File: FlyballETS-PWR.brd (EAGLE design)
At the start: 48.3 x 50.8 mm, 8 parts

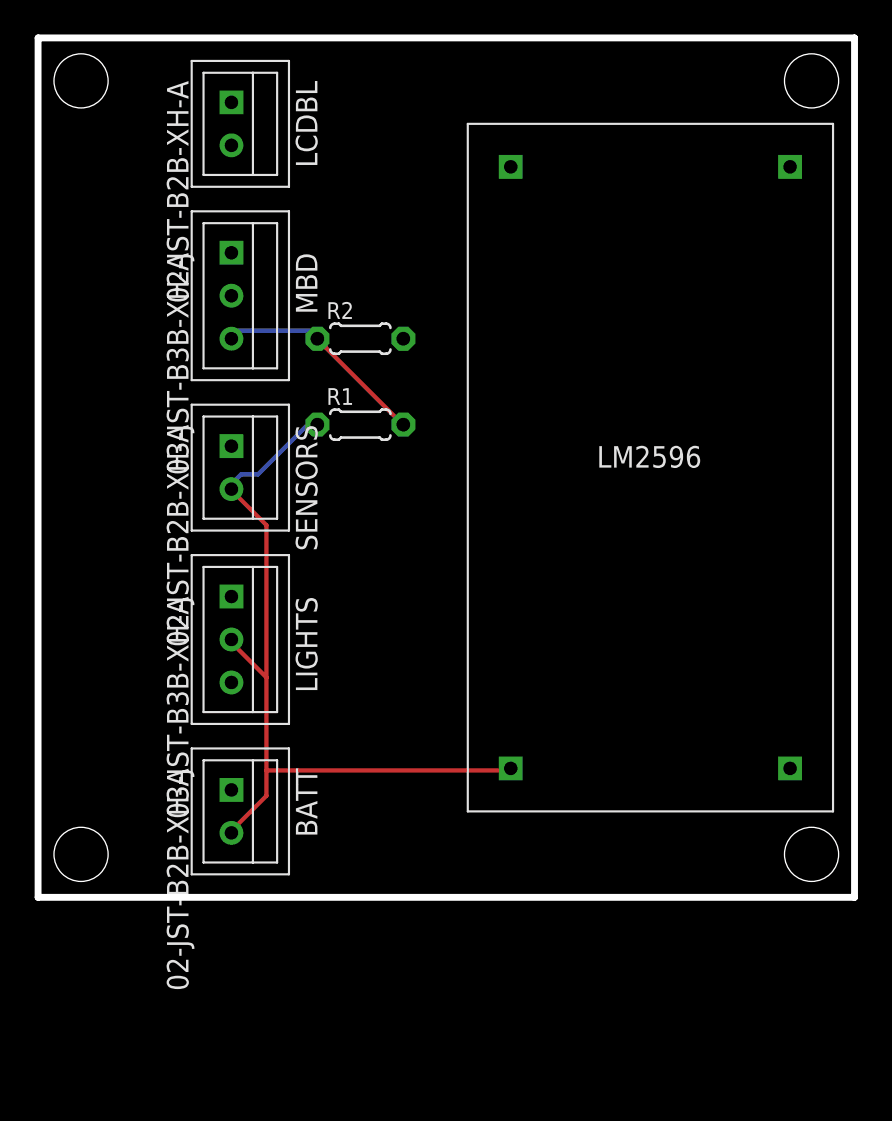
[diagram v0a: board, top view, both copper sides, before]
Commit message: Updated drawings and added PNG exports
- Added frames around drawings to make it look neater
- Added PNG export files so people who don't have EAGLE can see
everything
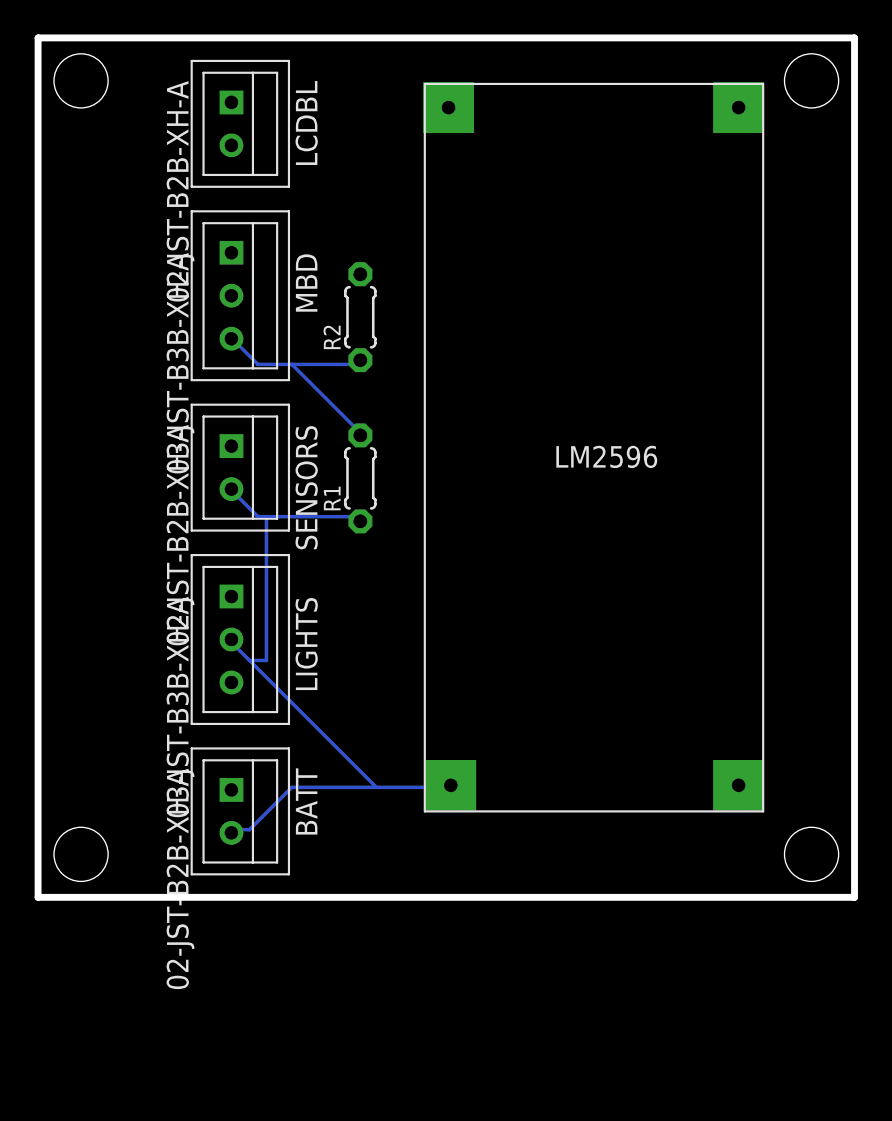
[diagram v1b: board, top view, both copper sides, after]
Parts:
- removed U$3: LM2596-BOARD, _custom:LM2596-BOARD
- added U$1: LM2596-BOARD, _custom:LM2596-BOARD
- added U$2: (no value), frames:A5L-LOC
- moved R1 3.18 mm to (19.1, 24.8), turned to 90 degrees
- moved R2 1.27 mm to (19.1, 34.3), turned to 90 degrees
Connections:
- net +12V: now also U$1.VIN; no longer U$3.VIN
- net +5V: now also U$1.VOUT; no longer U$3.VOUT
- net GND: now also U$1.GND@1, U$1.GND@2; no longer U$3.GND@1, U$3.GND@2
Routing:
- net +12V: track 46.4 -> 44.5 mm
- net N$1: track 13.4 -> 14.3 mm
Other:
- board text added: "Alex Goris"
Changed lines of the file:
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@@
 http://bit.ly/1ErZ5QD
 LICENSE: CC-BY-SA</text>
+<text x="77.47" y="-27.94" size="2.54" layer="48">Alex Goris</text>
+<text x="25.4" y="-40.64" size="2.54" layer="48">FlyballETS
+PowerBoard v1
+http://bit.ly/1ErZ5QD
+LICENSE: CC-BY-SA</text>
+<dimension x1="48.26" y1="0" x2="48.26" y2="50.8" x3="58.42" y3="25.4" textsize="1.778" layer="48"/>
+<dimension x1="48.26" y1="50.8" x2="0" y2="50.8" x3="24.13" y3="60.96" textsize="1.778" layer="48"/>
 </plain>
 <attributes>
@@
 <element name="LIGHTS" library="bt_con-jst-xh" package="B3B-XH" value="03-JST-B3B-XH-A" x="11.43" y="15.24" rot="R270"/>
 <element name="MBD" library="bt_con-jst-xh" package="B3B-XH" value="03-JST-B3B-XH-A" x="11.43" y="35.56" rot="R270"/>
-<element name="R1" library="resistor" package="0204/5" value="70k" x="19.05" y="27.94"/>
-<element name="R2" library="resistor" package="0204/5" value="50k" x="19.05" y="33.02"/>
+<element name="R1" library="resistor" package="0204/5" value="70k" x="19.05" y="24.765" rot="R90"/>
+<element name="R2" library="resistor" package="0204/5" value="50k" x="19.05" y="34.29" rot="R90"/>
 <element name="SENSORS" library="bt_con-jst-xh" package="B2B-XH" value="02-JST-B2B-XH-A" x="11.43" y="24.13" rot="R270"/>
-<element name="U$3" library="_custom" package="LM2596-BOARD" value="LM2596-BOARD" x="25.4" y="5.08"/>
+<element name="U$1" library="_custom" package="LM2596-BOARD" value="LM2596-BOARD" x="22.86" y="5.08"/>
+<element name="U$2" library="frames" package="A5L-LOC" value="" x="-63.5" y="-48.26"/>
 </elements>
 <signals>
 <signal name="+5V">
-<contactref element="U$3" pad="VOUT"/>
 <contactref element="LIGHTS" pad="P$3"/>
 <contactref element="MBD" pad="P$2"/>
@@
 <vertex x="0" y="0"/>
 </polygon>
+<contactref element="U$1" pad="VOUT"/>
 </signal>
 <signal name="GND">
 <contactref element="BATT" pad="P$1"/>
-<contactref element="U$3" pad="GND@1"/>
 <contactref element="SENSORS" pad="P$1"/>
 <contactref element="LIGHTS" pad="P$1"/>
@@
 <contactref element="R2" pad="2"/>
 <contactref element="LCDBL" pad="P$1"/>
-<contactref element="U$3" pad="GND@2"/>
 <polygon width="0.4064" layer="16">
 <vertex x="0" y="50.8"/>
@@
 <vertex x="0" y="0"/>
 </polygon>
+<contactref element="U$1" pad="GND@1"/>
+<contactref element="U$1" pad="GND@2"/>
 </signal>
 <signal name="+12V">
 <contactref element="BATT" pad="P$2"/>
-<contactref element="U$3" pad="VIN"/>
 <contactref element="SENSORS" pad="P$2"/>
 <contactref element="LIGHTS" pad="P$2"/>
 <contactref element="R1" pad="1"/>
-<wire x1="12" y1="25" x2="11.5" y2="24.5" width="0.254" layer="16"/>
-<wire x1="13" y1="25" x2="12" y2="25" width="0.254" layer="16"/>
-<wire x1="16" y1="28" x2="13" y2="25" width="0.254" layer="16"/>
-<wire x1="16.5" y1="28" x2="16" y2="28" width="0.254" layer="16"/>
-<wire x1="11.5" y1="24.5" x2="11.43" y2="24.13" width="0.254" layer="16"/>
-<wire x1="16.5" y1="28" x2="16.51" y2="27.94" width="0.254" layer="16"/>
-<wire x1="13.5" y1="6" x2="11.5" y2="4" width="0.254" layer="1"/>
-<wire x1="13.5" y1="13" x2="13.5" y2="7.5" width="0.254" layer="1"/>
-<wire x1="13.5" y1="7.5" x2="13.5" y2="6" width="0.254" layer="1"/>
-<wire x1="11.5" y1="15" x2="13.5" y2="13" width="0.254" layer="1"/>
-<wire x1="11.5" y1="4" x2="11.43" y2="3.81" width="0.254" layer="1"/>
-<wire x1="11.5" y1="15" x2="11.43" y2="15.24" width="0.254" layer="1"/>
-<wire x1="13.5" y1="7.5" x2="27.5" y2="7.5" width="0.254" layer="1"/>
-<wire x1="27.5" y1="7.5" x2="27.94" y2="7.62" width="0.254" layer="1"/>
-<wire x1="13.5" y1="22" x2="11.5" y2="24" width="0.254" layer="1"/>
-<wire x1="13.5" y1="13" x2="13.5" y2="22" width="0.254" layer="1"/>
-<wire x1="11.5" y1="24" x2="11.43" y2="24.13" width="0.254" layer="1"/>
+<contactref element="U$1" pad="VIN"/>
+<wire x1="13" y1="22.5" x2="11.5" y2="24" width="0.2032" layer="16"/>
+<wire x1="19" y1="22.5" x2="13.5" y2="22.5" width="0.2032" layer="16"/>
+<wire x1="13.5" y1="22.5" x2="13" y2="22.5" width="0.2032" layer="16"/>
+<wire x1="11.5" y1="24" x2="11.43" y2="24.13" width="0.2032" layer="16"/>
+<wire x1="19" y1="22.5" x2="19.05" y2="22.225" width="0.2032" layer="16"/>
+<wire x1="12.5" y1="4" x2="11.5" y2="4" width="0.2032" layer="16"/>
+<wire x1="15" y1="6.5" x2="12.5" y2="4" width="0.2032" layer="16"/>
+<wire x1="24" y1="6.5" x2="20" y2="6.5" width="0.2032" layer="16"/>
+<wire x1="20" y1="6.5" x2="15" y2="6.5" width="0.2032" layer="16"/>
+<wire x1="11.5" y1="4" x2="11.43" y2="3.81" width="0.2032" layer="16"/>
+<wire x1="24" y1="6.5" x2="24.4" y2="6.62" width="0.2032" layer="16"/>
+<wire x1="20" y1="6.5" x2="12.5" y2="14" width="0.2032" layer="16"/>
+<wire x1="12.5" y1="14" x2="11.5" y2="15" width="0.2032" layer="16"/>
+<wire x1="11.5" y1="15" x2="11.43" y2="15.24" width="0.2032" layer="16"/>
+<wire x1="13.5" y1="14" x2="13.5" y2="22.5" width="0.2032" layer="16"/>
+<wire x1="12.5" y1="14" x2="13.5" y2="14" width="0.2032" layer="16"/>
 </signal>
 <signal name="N$1">
@@
 <contactref element="R2" pad="1"/>
 <contactref element="MBD" pad="P$3"/>
-<wire x1="16.5" y1="33.5" x2="11.5" y2="33.5" width="0.254" layer="16"/>
-<wire x1="11.5" y1="33.5" x2="11.43" y2="33.02" width="0.254" layer="16"/>
-<wire x1="16.5" y1="33.5" x2="16.51" y2="33.02" width="0.254" layer="16"/>
-<wire x1="17" y1="32.5" x2="21.5" y2="28" width="0.254" layer="1"/>
-<wire x1="17" y1="33" x2="17" y2="32.5" width="0.254" layer="1"/>
-<wire x1="21.5" y1="28" x2="21.59" y2="27.94" width="0.254" layer="1"/>
-<wire x1="17" y1="33" x2="16.51" y2="33.02" width="0.254" layer="1"/>
+<wire x1="13" y1="31.5" x2="11.5" y2="33" width="0.2032" layer="16"/>
+<wire x1="19" y1="31.5" x2="15" y2="31.5" width="0.2032" layer="16"/>
+<wire x1="15" y1="31.5" x2="13" y2="31.5" width="0.2032" layer="16"/>
+<wire x1="11.5" y1="33" x2="11.43" y2="33.02" width="0.2032" layer="16"/>
+<wire x1="19" y1="31.5" x2="19.05" y2="31.75" width="0.2032" layer="16"/>
+<wire x1="15" y1="31.5" x2="19" y2="27.5" width="0.2032" layer="16"/>
+<wire x1="19" y1="27.5" x2="19.05" y2="27.305" width="0.2032" layer="16"/>
 </signal>
 </signals>

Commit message: v2 release of remaining boards.
- Lightsboard: Corrected swapped pin connections on L2 side and made
smaller
- Powerboard: Made smaller and added descriptions for LM2596 board
- Sensorboard: Made smaller
- All boards: Removed JST connector type names
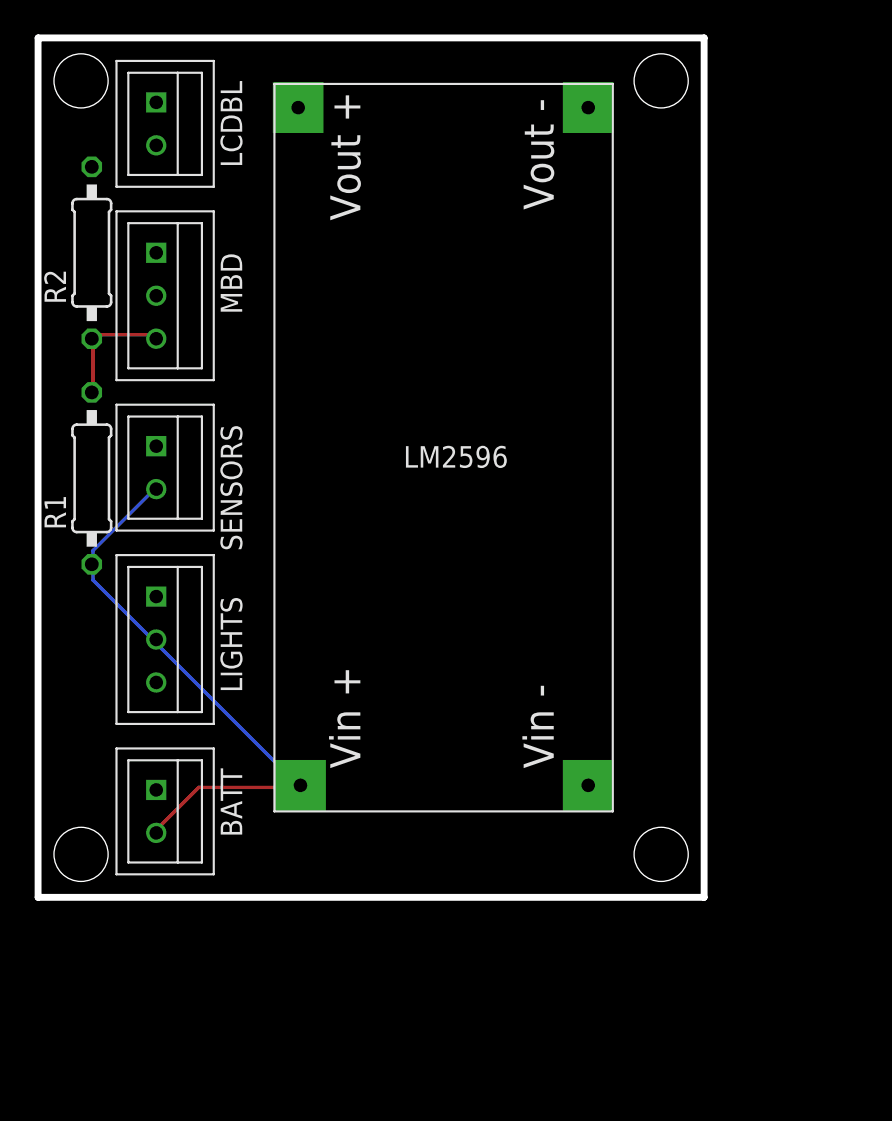
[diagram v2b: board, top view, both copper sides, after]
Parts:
- R1, R2: device resistor:0204/5 -> resistor:0207/10
- moved R2 16.3 mm to (3.17, 38.1)
- moved R1 15.9 mm to (3.17, 24.8)
- moved U$1 8.89 mm to (14.0, 5.08)
- moved BATT 4.44 mm to (6.99, 3.81)
- moved LCDBL 4.44 mm to (6.99, 44.5)
- moved LIGHTS 4.44 mm to (6.99, 15.2)
- moved MBD 4.44 mm to (6.99, 35.6)
- moved SENSORS 4.44 mm to (6.99, 24.1)
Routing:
- net +12V: track 44.5 -> 34.4 mm
- net N$1: track 14.3 -> 7.32 mm
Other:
- board size 48.3 x 50.8 mm -> 39.4 x 50.8 mm
- board text added: "FlyballETS PowerBoard v2 http://bit.ly/1ErZ5QD LICENSE: CC-BY-SA"
- board text added: "Vin +"
- board text added: "Vin -"
- board text added: "Vout +"
- board text added: "Vout -"
- board text removed: "FlyballETS PowerBoard v1 http://bit.ly/1ErZ5QD LICENSE: CC-BY-SA"

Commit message: Changed resistor values to more practical ones
Changed R1 to 5.6kOhm, R2 to 3.9kOhm. These are common values in
resistor assortments. Fixes #2
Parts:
- R1: value 70k -> 5.6k
- R2: value 50k -> 3.9k
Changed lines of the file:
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@@
 <attribute name="NAME" x="10.795" y="38.1" size="1.27" layer="21" rot="R270"/>
 </element>
-<element name="R1" library="resistor" package="0207/10" value="70k" x="3.175" y="24.765" rot="R90"/>
-<element name="R2" library="resistor" package="0207/10" value="50k" x="3.175" y="38.1" rot="R90"/>
+<element name="R1" library="resistor" package="0207/10" value="5.6k" x="3.175" y="24.765" rot="R90"/>
+<element name="R2" library="resistor" package="0207/10" value="3.9k" x="3.175" y="38.1" rot="R90"/>
 <element name="SENSORS" library="bt_con-jst-xh" package="B2B-XH" value="02-JST-B2B-XH-A" x="6.985" y="24.13" smashed="yes" rot="R270">
 <attribute name="NAME" x="10.795" y="27.94" size="1.27" layer="21" rot="R270"/>
